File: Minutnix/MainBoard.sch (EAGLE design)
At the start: 131 parts, among them IC1 MEGA8-AI, IC10 TPIC6C596PW, IC11 TPIC6C596PW, IC12 TPIC6C596PW, IC13 TPIC6C596PW, IC2 TPIC6C596PW, IC3 TPIC6C596PW, IC4 TPIC6C596PW, IC5 TPIC6C596PW, IC6 TP4056, IC8 FT230XS, IC9 SC4503, Q4 32.768kHz, T1 DMN3024LSD

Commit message: Updated pinout
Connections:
- net BUZZ: now also ATMEGA328P.PB1; no longer ATMEGA328P.PD5
- net D_RCK: now also ATMEGA328P.PB0, IC1.PB0(ICP); no longer ATMEGA328P.PB1, IC1.PD5(T1)
- net L1: now also ATMEGA328P.PC0, IC1.PC0(ADC0); no longer ATMEGA328P.PD4, IC1.PD4(XCK/T0)
- net L2: now also ATMEGA328P.PC1, IC1.PC1(ADC1); no longer ATMEGA328P.PD3, IC1.PD3(INT1)
- net L3: now also ATMEGA328P.PC2, IC1.PC2(ADC2); no longer ATMEGA328P.PC3
- net L4: now also ATMEGA328P.PC3; no longer ATMEGA328P.PC2, IC1.PC2(ADC2)
- net L5: no longer ATMEGA328P.PC1, IC1.PC1(ADC1)
- net L6: no longer ATMEGA328P.PC0, IC1.PC0(ADC0)
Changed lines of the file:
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@@
 <plain>
 <wire x1="92.07" y1="129.54" x2="92.07" y2="24.13" width="0.1" layer="94"/>
-<text x="38.28" y="127.4" size="1.778" layer="94">Atmega8 version</text>
-<text x="130.27" y="127.14" size="1.778" layer="94">Atmega328p version</text>
+<text x="20.5" y="122.32" size="5.08" layer="94">Atmega8 version</text>
+<text x="107.41" y="122.06" size="5.08" layer="94">Atmega328p version</text>
 <text x="140.7" y="20.4" size="2.54" layer="94">CONTROL</text>
 </plain>
@@
 <net name="D_RCK" class="0">
 <segment>
-<wire x1="106.68" y1="78.74" x2="121.92" y2="78.74" width="0.1524" layer="91"/>
-<label x="106.68" y="78.74" size="1.778" layer="95"/>
-<pinref part="ATMEGA328P" gate="A" pin="PB1"/>
-</segment>
-<segment>
-<wire x1="69.52" y1="71.12" x2="84.76" y2="71.12" width="0.1524" layer="91"/>
-<label x="84.76" y="71.12" size="1.778" layer="95" rot="MR0"/>
-<pinref part="IC1" gate="G$1" pin="PD5(T1)"/>
+<wire x1="106.68" y1="81.28" x2="121.92" y2="81.28" width="0.1524" layer="91"/>
+<label x="106.68" y="81.28" size="1.778" layer="95"/>
+<pinref part="ATMEGA328P" gate="A" pin="PB0"/>
+</segment>
+<segment>
+<wire x1="69.52" y1="60.96" x2="84.76" y2="60.96" width="0.1524" layer="91"/>
+<label x="84.76" y="60.96" size="1.778" layer="95" rot="MR0"/>
+<pinref part="IC1" gate="G$1" pin="PB0(ICP)"/>
 </segment>
 </net>
 <net name="BUZZ" class="0">
-<segment>
-<wire x1="172.72" y1="71.12" x2="157.48" y2="71.12" width="0.1524" layer="91"/>
-<pinref part="ATMEGA328P" gate="A" pin="PD5"/>
-<label x="172.72" y="71.12" size="1.778" layer="95" rot="MR0"/>
-</segment>
 <segment>
 <wire x1="84.76" y1="58.42" x2="69.52" y2="58.42" width="0.1524" layer="91"/>
@@
 <pinref part="IC1" gate="G$1" pin="PB1(OC1A)"/>
 </segment>
+<segment>
+<wire x1="121.92" y1="78.74" x2="106.68" y2="78.74" width="0.1524" layer="91"/>
+<label x="106.68" y="78.74" size="1.778" layer="95"/>
+<pinref part="ATMEGA328P" gate="A" pin="PB1"/>
+</segment>
 </net>
 <net name="EXP_SDA" class="0">
@@
 </segment>
 <segment>
+<wire x1="157.48" y1="99.06" x2="172.72" y2="99.06" width="0.1524" layer="91"/>
+<label x="172.72" y="99.06" size="1.778" layer="255" rot="MR0"/>
+<pinref part="ATMEGA328P" gate="A" pin="PC2"/>
+</segment>
+<segment>
+<pinref part="IC1" gate="G$1" pin="PC2(ADC2)"/>
+<wire x1="69.52" y1="101.6" x2="84.76" y2="101.6" width="0.1524" layer="91"/>
+<label x="84.76" y="101.6" size="1.778" layer="255" rot="MR0"/>
+</segment>
+</net>
+<net name="L4" class="0">
+<segment>
 <wire x1="157.48" y1="96.52" x2="172.72" y2="96.52" width="0.1524" layer="91"/>
 <label x="172.72" y="96.52" size="1.778" layer="255" rot="MR0"/>
 <pinref part="ATMEGA328P" gate="A" pin="PC3"/>
-</segment>
-</net>
-<net name="L4" class="0">
-<segment>
-<pinref part="IC1" gate="G$1" pin="PC2(ADC2)"/>
-<wire x1="69.52" y1="101.6" x2="84.76" y2="101.6" width="0.1524" layer="91"/>
-<label x="84.76" y="101.6" size="1.778" layer="255" rot="MR0"/>
-</segment>
-<segment>
-<wire x1="157.48" y1="99.06" x2="172.72" y2="99.06" width="0.1524" layer="91"/>
-<label x="172.72" y="99.06" size="1.778" layer="255" rot="MR0"/>
-<pinref part="ATMEGA328P" gate="A" pin="PC2"/>
-</segment>
-</net>
-<net name="L5" class="0">
-<segment>
-<pinref part="IC1" gate="G$1" pin="PC1(ADC1)"/>
-<wire x1="69.52" y1="104.14" x2="84.76" y2="104.14" width="0.1524" layer="91"/>
-<label x="84.76" y="104.14" size="1.778" layer="255" rot="MR0"/>
-</segment>
-<segment>
-<wire x1="157.48" y1="101.6" x2="172.72" y2="101.6" width="0.1524" layer="91"/>
-<label x="172.72" y="101.6" size="1.778" layer="255" rot="MR0"/>
-<pinref part="ATMEGA328P" gate="A" pin="PC1"/>
-</segment>
-</net>
-<net name="L6" class="0">
-<segment>
-<pinref part="IC1" gate="G$1" pin="PC0(ADC0)"/>
-<wire x1="69.52" y1="106.68" x2="84.76" y2="106.68" width="0.1524" layer="91"/>
-<label x="84.76" y="106.68" size="1.778" layer="255" rot="MR0"/>
-</segment>
-<segment>
-<wire x1="157.48" y1="104.14" x2="172.72" y2="104.14" width="0.1524" layer="91"/>
-<label x="172.72" y="104.14" size="1.778" layer="255" rot="MR0"/>
-<pinref part="ATMEGA328P" gate="A" pin="PC0"/>
-</segment>
-</net>
-<net name="L1" class="0">
-<segment>
-<wire x1="157.48" y1="73.66" x2="172.72" y2="73.66" width="0.1524" layer="91"/>
-<label x="172.72" y="73.66" size="1.778" layer="255" rot="MR0"/>
-<pinref part="ATMEGA328P" gate="A" pin="PD4"/>
-</segment>
-<segment>
-<wire x1="69.52" y1="73.66" x2="84.76" y2="73.66" width="0.1524" layer="91"/>
-<label x="84.76" y="73.66" size="1.778" layer="255" rot="MR0"/>
-<pinref part="IC1" gate="G$1" pin="PD4(XCK/T0)"/>
-</segment>
-</net>
-<net name="L2" class="0">
-<segment>
-<wire x1="157.48" y1="76.2" x2="172.72" y2="76.2" width="0.1524" layer="91"/>
-<label x="172.72" y="76.2" size="1.778" layer="255" rot="MR0"/>
-<pinref part="ATMEGA328P" gate="A" pin="PD3"/>
-</segment>
-<segment>
-<wire x1="69.52" y1="76.2" x2="84.76" y2="76.2" width="0.1524" layer="91"/>
-<label x="84.76" y="76.2" size="1.778" layer="255" rot="MR0"/>
-<pinref part="IC1" gate="G$1" pin="PD3(INT1)"/>
 </segment>
 </net>
@@
 <wire x1="121.92" y1="53.34" x2="119.38" y2="53.34" width="0.1524" layer="91"/>
 <wire x1="119.38" y1="53.34" x2="119.38" y2="55.88" width="0.1524" layer="91"/>
+</segment>
+</net>
+<net name="L1" class="0">
+<segment>
+<wire x1="157.48" y1="104.14" x2="172.72" y2="104.14" width="0.1524" layer="91"/>
+<label x="172.72" y="104.14" size="1.778" layer="255" rot="MR0"/>
+<pinref part="ATMEGA328P" gate="A" pin="PC0"/>
+</segment>
+<segment>
+<pinref part="IC1" gate="G$1" pin="PC0(ADC0)"/>
+<wire x1="69.52" y1="106.68" x2="84.76" y2="106.68" width="0.1524" layer="91"/>
+<label x="84.76" y="106.68" size="1.778" layer="255" rot="MR0"/>
+</segment>
+</net>
+<net name="L2" class="0">
+<segment>
+<wire x1="157.48" y1="101.6" x2="172.72" y2="101.6" width="0.1524" layer="91"/>
+<label x="172.72" y="101.6" size="1.778" layer="255" rot="MR0"/>
+<pinref part="ATMEGA328P" gate="A" pin="PC1"/>
+</segment>
+<segment>
+<pinref part="IC1" gate="G$1" pin="PC1(ADC1)"/>
+<wire x1="69.52" y1="104.14" x2="84.76" y2="104.14" width="0.1524" layer="91"/>
+<label x="84.76" y="104.14" size="1.778" layer="255" rot="MR0"/>
 </segment>
 </net>
@@
 </instance>
 <instance part="C31" gate="G$1" x="29.7" y="64.62" smashed="yes">
-<attribute name="VALUE" x="30.843" y="60.0226" size="1.778" layer="96"/>
+<attribute name="VALUE" x="20.683" y="62.5626" size="1.778" layer="96"/>
 </instance>
 <instance part="SHOTTKYDIODE3" gate="G$1" x="37.32" y="62.08" smashed="yes" rot="R90">
-<attribute name="NAME" x="34.78" y="60.0226" size="1.778" layer="95" rot="MR0"/>
+<attribute name="NAME" x="60.18" y="62.5626" size="1.778" layer="95" rot="MR0"/>
 </instance>
 <instance part="FRAME3" gate="G$1" x="0" y="0" smashed="yes">

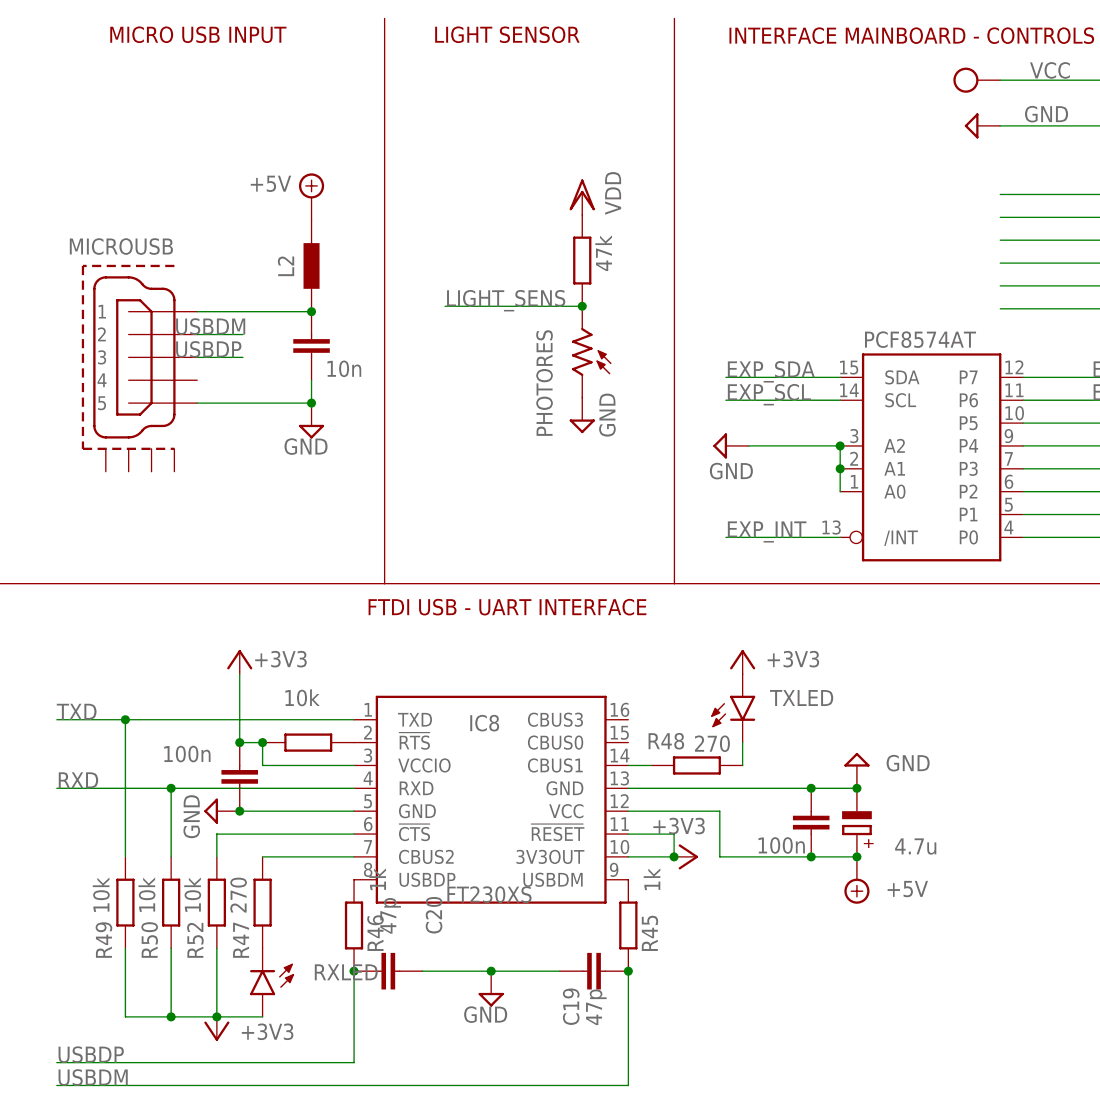
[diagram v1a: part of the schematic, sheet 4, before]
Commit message: Update MainBoard.sch
Corrected some values, added descriptions and some typos.
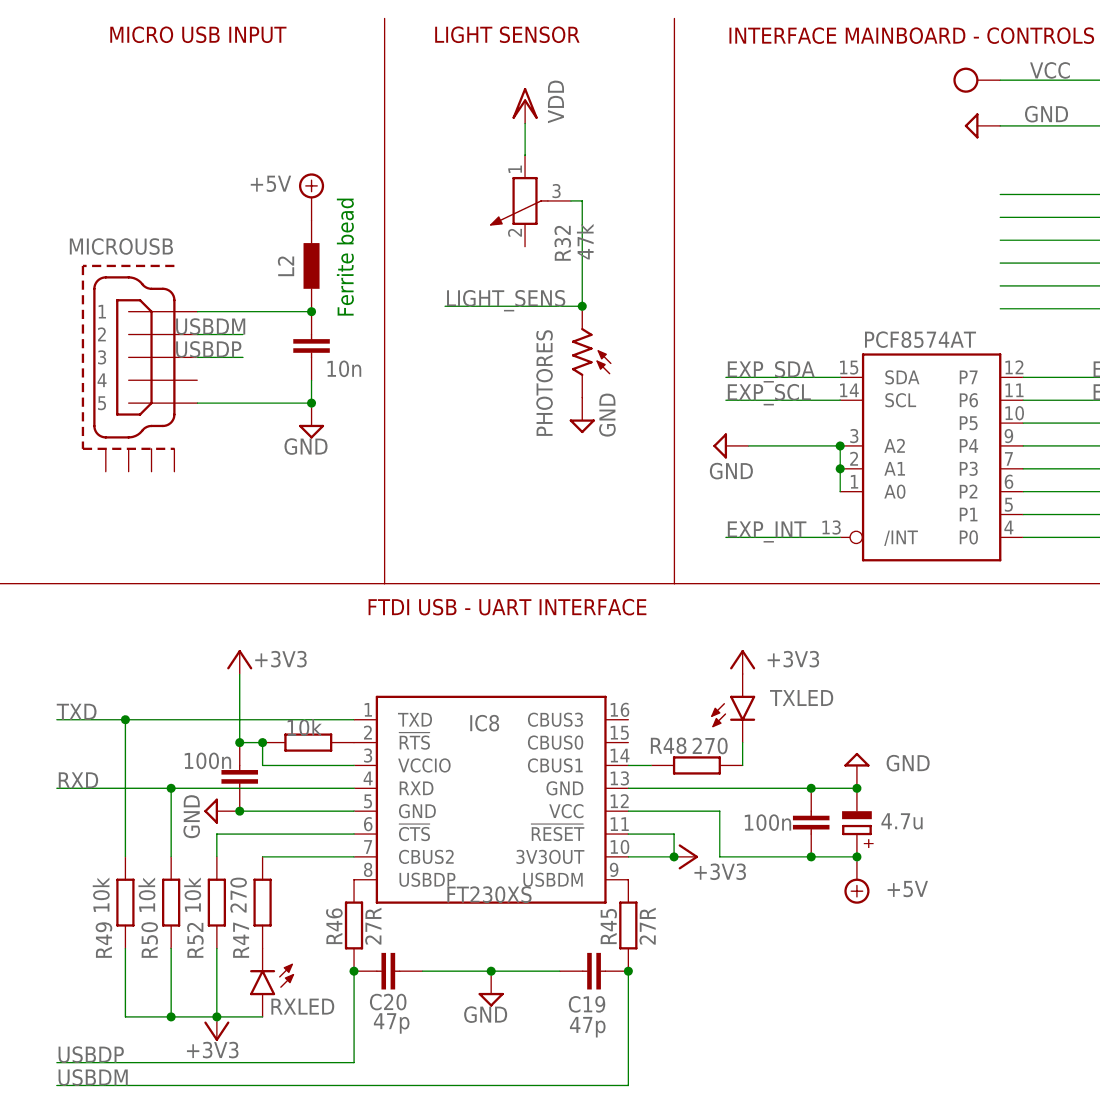
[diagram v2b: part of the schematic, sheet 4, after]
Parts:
- removed L5: BLM15HB121SN1, inductors:BLM15HB121SN1
- removed R31: 47k, rcl:R-EU_R1206
- added L1: 10uH, inductor-neosid:MS42
- added R32: 47k, rcl:POTENTIOMETER_PT-10
- R45, R46: value 1k -> 27R
- R53: value 15k4 -> 15k
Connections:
- net AVCC: now also L1.1; no longer L5.2
- net L3: no longer IC1.PC3(ADC3)
- net L4: now also IC1.PC3(ADC3)
- net LIGHT_SENS: now also R32.3; no longer R31.1
- net S_VCC: now also L1.2; no longer L5.1
- net VDD: now also R32.1; no longer R31.2
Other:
- note added: "Ferrite bead"
- note added: "L ~ 10uH"

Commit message: After review corrections
W programie LEDy od dwukropka sa kropkami dwoch srodkowych wyswietlaczy (wariant w ktorym segmenty wyswietlacza sa obslugiwane przez dwa osobbe rejestry przesuwny jest niekorzystny programowo)
Light sensor powinien byc podlaczony do PC0 [L1] (olewamy ADC6)
Czy na pewno podlaczenie TX ATmegi do TX FTDI ma sens? Nie powinno byc crossowania?  (oznaczenie TX dotyczy ATmegi)
Nowe podlaczenie pinow PCF na schematach (nie uzyc pinu P7)
Usunac przyciski z podswietleniem (przyciskow jest 5), 3 LEDy sygnalizujace wybrana opcje ustawien wlaczane stanem niskim na pinie ATmegi (P1 - P3)
Przycisk zwierajacy PD7 do masy na schemacie (dodaj do BOMu)
Czy jest pull-up na PC6 (RESET)?
Brakuje konektora do USBasp (wgranie bootloadera)
Niezaprogramowane piny z wyprowadzonymi padami
Podciagniecie pinu 7 ekspandera PCFa do VCC za posrednictwem rezystora 10k
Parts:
- removed B_GND, B_VCC, PAD1, PAD10, PAD11, PAD12, PAD13, PAD14, PAD2, PAD3, PAD4, PAD5, PAD6, PAD7, PAD8, PAD9: WIREPADSMD5-2,5, wirepad:WIREPADSMD5-2,5
- removed LED1, LED2: (no value), led:LED5MM
- added COLON1, COLON2: (no value), led:LED5MM
- added JP1, JP10, JP2, JP3, JP4, JP5, JP6, JP7, JP8, JP9: (no value), pinhead:PINHD-1X1
- added PROGRAMMING: SKHMPSE010, switch:SKHMPSE010
- added R31, R33, R42, R43, R44, R59, R60, R61: 4.7k, rcl:R-EU_01005
- added R62, R63, R64: 220, rcl:R-EU_01005
- added SJ1: (no value), jumper:SJ
- added SPI_JUMPERS: (no value), con-lstb:MA03-2
- added X1: FH12-12S-0.5SH, con-hirose:FH12-12S-0.5SH
- C9: value (none) -> 0.1uF
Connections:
- removed net B1: PAD1.P, U$1IC$1.P0
- removed net B2: PAD2.P, U$1IC$1.P1
- removed net B3: PAD3.P, U$1IC$1.P2
- removed net B4: PAD4.P, U$1IC$1.P3
- removed net B5: PAD5.P, U$1IC$1.P4
- removed net B6: PAD6.P, U$1IC$1.P5
- removed net L1: ATMEGA328P.PC0, IC1.PC0(ADC0), PAD9.P
- removed net L2: ATMEGA328P.PC1, IC1.PC1(ADC1), PAD10.P
- removed net L3: ATMEGA328P.PC2, IC1.PC2(ADC2), PAD11.P
- removed net L4: ATMEGA328P.PC3, IC1.PC3(ADC3), PAD12.P
- removed net L5: PAD13.P
- removed net L6: PAD14.P
- removed net N$121: IC3G$1.Q6, R34.2
- removed net N$122: IC3G$1.Q7, R35.2
- removed net N$43: IC2G$1.Q7, R8.2
- removed net N$74: IC4G$1.Q7, R22.2
- removed net N$97: LED1.C, R34.1
- new net COUNTER: R60.2, U$1IC$1.P0, X1-1.1
- new net L_COUNTER: ATMEGA328P.PC1, IC1.PC1(ADC1), R62.2
- new net L_VOLUME: ATMEGA328P.PC3, IC1.PC3(ADC3), R64.2
- new net L_WARNING: ATMEGA328P.PC2, IC1.PC2(ADC2), R63.2
- new net MISO: ATMEGA328P.PB4, IC1.PB4(MISO), SPI_JUMPERS.6
- new net N$12: COLON1.C, R34.1
- new net N$2: IC3G$1.Q7, R34.2
- new net N$20: IC4G$1.Q7, R35.2
- new net N$22: IC5G$1.Q0, R22.2
- new net N$26: R62.1, X1-8.1
- new net N$28: R63.1, X1-9.1
- new net N$29: R64.1, X1-10.1
- new net N$30: R61.2, SJ1.2
- new net N$4: IC3G$1.Q0, R8.2
- new net PLAY/PAUSE: R43.2, U$1IC$1.P3, X1-4.1
- new net STOP/RESET: R42.2, U$1IC$1.P4, X1-5.1
- new net S_VCC?: PROGRAMMING.2.1, PROGRAMMING.2.2
- new net UA1: ATMEGA328P.PD3, IC1.PD3(INT1), JP1.1
- new net UA2: ATMEGA328P.PD4, IC1.PD4(XCK/T0), JP2.1
- new net UA3: ATMEGA328P.PD5, IC1.PD5(T1), JP3.1
- new net UA4: ATMEGA328P.ADC6, IC1.ADC6, JP4.1
- new net UA5: ATMEGA328P.ADC7, IC1.ADC7, JP5.1
- new net UD1: IC2G$1.Q7, JP6.1
- new net UD2: IC5G$1.Q7, JP7.1
- new net UF1: IC8.CBUS0, JP9.1
- new net UF2: IC8.CBUS3, JP10.1
- new net UP1: JP8.1, SJ1.1, U$1IC$1.P7
- new net VDD1: LSDIGIT.CA1, LSDIGIT.CA8, LSDIGIT1.CA1, LSDIGIT1.CA8, MSDIGIT.CA1, MSDIGIT.CA8, MSDIGIT1.CA1, MSDIGIT1.CA8
- new net VOLUME: R44.2, U$1IC$1.P2, X1-3.1
- new net WARNING: R59.2, U$1IC$1.P1, X1-2.1
- net +5V: now also SPI_JUMPERS.5
- net D_SCK: now also SPI_JUMPERS.4
- net D_SI: now also SPI_JUMPERS.3
- net ENC_A: now also R33.2, U$1IC$1.P5, X1-6.1; no longer PAD7.P, U$1IC$1.P6
- net ENC_B: now also R31.2, U$1IC$1.P6, X1-7.1; no longer PAD8.P, U$1IC$1.P7
- net GND: now also MICROUSB.GND1, MICROUSB.GND2, MICROUSB.GND3, MICROUSB.GND4, PROGRAMMING.1.1, PROGRAMMING.1.2, PROGRAMMING.SH, SPI_JUMPERS.1, X1-12.1; no longer B_GND.P
- net LIGHT_SENS: now also ATMEGA328P.PC0, IC1.PC0(ADC0); no longer ATMEGA328P.ADC6, IC1.ADC6
- net N$120: now also COLON2.C; no longer LED2.C
- net N$58: now also IC3G$1.Q1; no longer IC3G$1.Q0
- net N$59: now also IC3G$1.Q2; no longer IC3G$1.Q1
- net N$60: now also IC3G$1.Q3; no longer IC3G$1.Q2
- net N$61: now also IC3G$1.Q4; no longer IC3G$1.Q3
- net N$62: now also IC3G$1.Q5; no longer IC3G$1.Q4
- net N$63: now also IC3G$1.Q6; no longer IC3G$1.Q5
- net N$75: now also IC5G$1.Q1; no longer IC5G$1.Q0
- net N$76: now also IC5G$1.Q2; no longer IC5G$1.Q1
- net N$77: now also IC5G$1.Q3; no longer IC5G$1.Q2
- net N$94: now also IC5G$1.Q4; no longer IC5G$1.Q3
- net N$95: now also IC5G$1.Q5; no longer IC5G$1.Q4
- net N$96: now also IC5G$1.Q6; no longer IC5G$1.Q5
- net RESET: now also SPI_JUMPERS.2
- net RXD: now also IC8.TXD, R49.1; no longer IC8.RXD, R50.1
- net TXD: now also IC8.RXD, R50.1; no longer IC8.TXD, R49.1
- net VCC: now also COLON1.A, COLON2.A, R31.1, R33.1, R42.1, R43.1, R44.1, R59.1, R60.1, R61.1, X1-11.1; no longer B_VCC.P, LED1.A, LED2.A
- net VDD: no longer LSDIGIT.CA1, LSDIGIT.CA8, LSDIGIT1.CA1, LSDIGIT1.CA8, MSDIGIT.CA1, MSDIGIT.CA8, MSDIGIT1.CA1, MSDIGIT1.CA8
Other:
- note added: "Programming"
- note added: "Unused pins jumpers"
